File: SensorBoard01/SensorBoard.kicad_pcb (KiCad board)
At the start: 2 copper layers, 24.1 x 29.2 mm, 29 parts, among them U1 DS7505, U2 74HC595-PWR

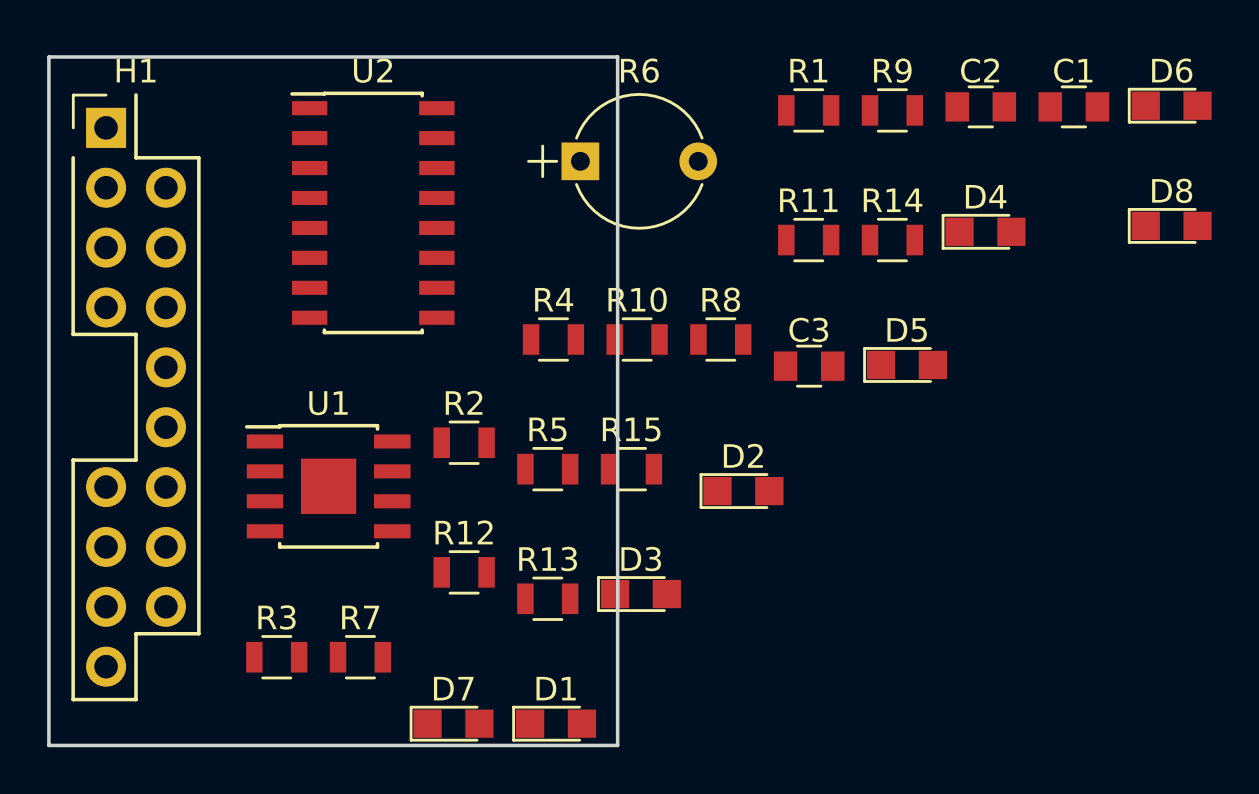
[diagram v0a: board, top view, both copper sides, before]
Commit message: Completed the layout for the CE_Header sensor board
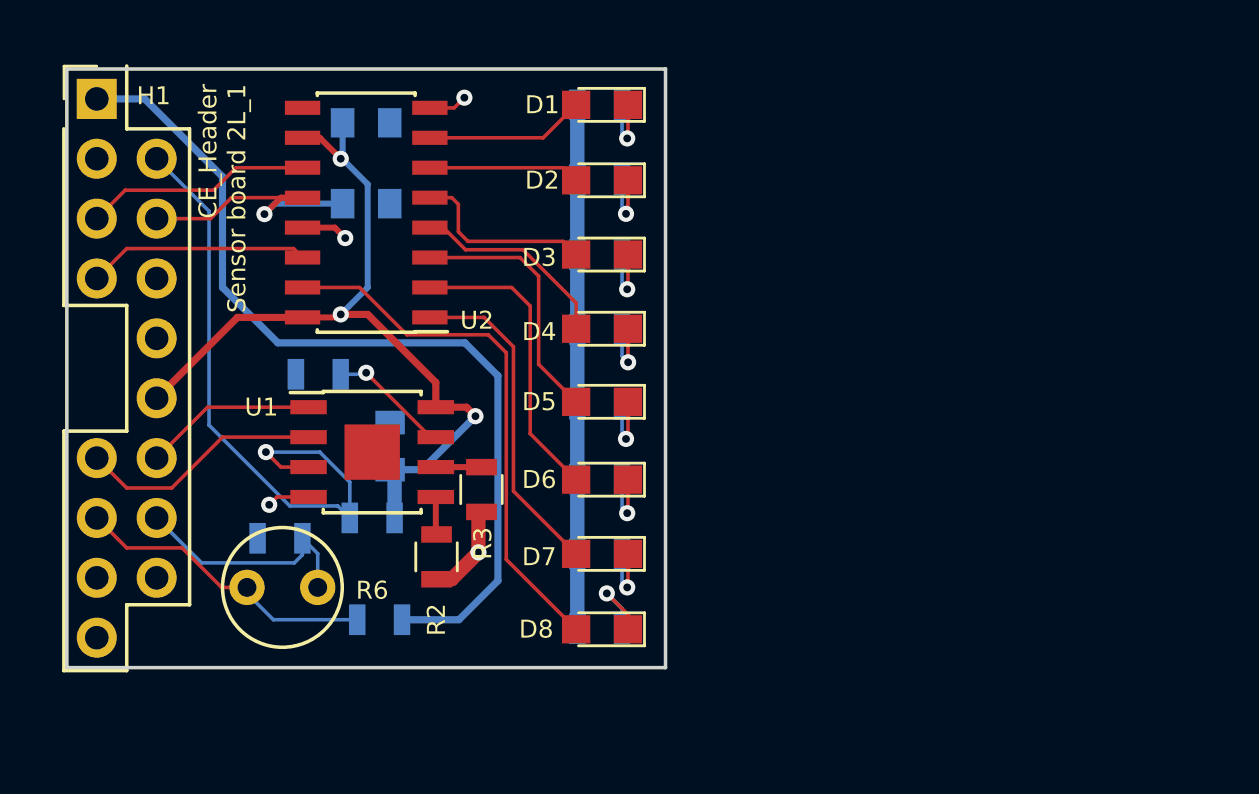
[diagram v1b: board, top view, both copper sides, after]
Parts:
- C1, C2, C3, R1, R10, R11, R12, R13, R14, R15, R4, R5, R7, R8, R9: moved to B.Cu
- R6: footprint Capacitors_ThroughHole:CP_Radial_Tantal_D5.5mm_P5.00mm -> CE_Header:Photo_Resistor_LDR01
- moved C1 32.4 mm to (168.1, 124.5), turned to 270 degrees
- moved D8 29.6 mm to (177.1, 132.2), turned to 180 degrees
- moved D6 28.9 mm to (177.1, 125.9), turned to 180 degrees
- moved C2 26.4 mm to (167.1, 114.2)
- moved D1 26.3 mm to (177.1, 110.0), turned to 180 degrees
- moved R1 25.3 mm to (167.4, 127.5), turned to 180 degrees
- moved R6 22.1 mm to (163.6, 130.5)
- moved C3 21.4 mm to (167.1, 110.7), turned to 180 degrees
- moved R14 18.2 mm to (177.0, 129.0)
- moved D4 16.8 mm to (177.1, 119.5), turned to 180 degrees
- moved D3 14.5 mm to (177.1, 116.3), turned to 180 degrees
- moved D2 14.5 mm to (177.1, 113.2), turned to 180 degrees
- moved D5 13.0 mm to (177.1, 122.6), turned to 180 degrees
- moved R9 12.8 mm to (177.0, 113.2)
- moved R3 11.2 mm to (172.0, 126.3), turned to 270 degrees
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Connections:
- H1 pad 1: Net-(H1-Pad1) -> /5V
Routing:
- net /5V: track 0.00 -> 38.1 mm
- net /3V3: track 0.00 -> 35.2 mm, vias 0 -> 3
- net GND: track 0.00 -> 32.0 mm, vias 0 -> 4
- net /O.S: track 0.00 -> 27.5 mm, vias 0 -> 1
- net Net-(D8-Pad2): track 0.00 -> 22.8 mm
- net Net-(D7-Pad2): track 0.00 -> 14.0 mm
- net /PT_TOP: track 0.00 -> 13.0 mm
- net Net-(D6-Pad2): track 0.00 -> 12.8 mm
- net /latchPin: track 0.00 -> 12.7 mm, vias 0 -> 1
- net Net-(D5-Pad2): track 0.00 -> 10.9 mm
- net /SCL: track 0.00 -> 10.4 mm
- net /PR_BOT: track 0.00 -> 10.2 mm
- net /clockPin: track 0.00 -> 9.62 mm
- net /dataPin: track 0.00 -> 9.41 mm
- net Net-(D4-Pad2): track 0.00 -> 8.63 mm
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- added copper zone on B.Cu, net GND
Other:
- board size 24.1 x 29.2 mm -> 25.4 x 25.4 mm
- net class Default: clearance 0.2 -> 0.1524; trace_width 0.25 -> 0.1524; via_dia 0.6 -> 0.6858; via_drill 0.4 -> 0.3302
- rule pad_to_mask_clearance: 0.2 -> 0
- rule trace_clearance: 0.2 -> 0.1524
- rule trace_min: 0.2 -> 0.1524
- rule via_min_drill: 0.3 -> 0.3302
- rule via_min_size: 0.4 -> 0.6858
- board text added: "CE_Header Sensor board 2L_1"
